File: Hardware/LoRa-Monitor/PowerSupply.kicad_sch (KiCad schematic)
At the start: 0 parts

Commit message: Fixed Power and Ground on the Interface nodes
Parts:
- added U8: IRM-03-5, Converter_ACDC:Converter_ACDC_MeanWell_IRM-03-xx_THT, symbol Converter_ACDC:IRM-03-5
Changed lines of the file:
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@@
 	(generator_version "10.0")
 	(paper "A4")
+	(symbol
+		(lib_id "Converter_ACDC:IRM-03-5")
+		(at 67.31 53.34 0)
+		(unit 1)
+		(body_style 1)
+		(exclude_from_sim no)
+		(in_bom yes)
+		(on_board yes)
+		(in_pos_files yes)
+		(dnp no)
+		(fields_autoplaced yes)
+		(property "Reference" "U8"
+			(at 67.31 43.18 0)
+			(show_name no)
+			(do_not_autoplace no)
+			(effects
+				(font
+					(size 1.27 1.27)
+				)
+			)
+		)
+		(property "Value" "IRM-03-5"
+			(at 67.31 45.72 0)
+			(show_name no)
+			(do_not_autoplace no)
+			(effects
+				(font
+					(size 1.27 1.27)
+				)
+			)
+		)
+		(property "Footprint" "Converter_ACDC:Converter_ACDC_MeanWell_IRM-03-xx_THT"
+			(at 67.31 62.23 0)
+			(hide yes)
+			(show_name no)
+			(do_not_autoplace no)
+			(effects
+				(font
+					(size 1.27 1.27)
+				)
+			)
+		)
+		(property "Datasheet" "https://www.meanwell.com/Upload/PDF/IRM-03/IRM-03-SPEC.PDF"
+			(at 67.31 63.5 0)
+			(hide yes)
+			(show_name no)
+			(do_not_autoplace no)
+			(effects
+				(font
+					(size 1.27 1.27)
+				)
+			)
+		)
+		(property "Description" "5V, 600mA, 3W, Isolated, AC-DC, IRM03"
+			(at 67.31 53.34 0)
+			(hide yes)
+			(show_name no)
+			(do_not_autoplace no)
+			(effects
+				(font
+					(size 1.27 1.27)
+				)
+			)
+		)
+		(pin "3"
+		)
+		(pin "1"
+		)
+		(pin "16"
+		)
+		(pin "14"
+		)
+		(pin "5"
+		)
+		(instances
+			(project "LoRa-Monitor"
+				(path "/7510cc7d-c141-46d4-8947-7def3af8cf35/e98113b5-abe6-4cd1-ae05-96bff57301ff"
+					(reference "U8")
+					(unit 1)
+				)
+			)
+		)
+	)
 )

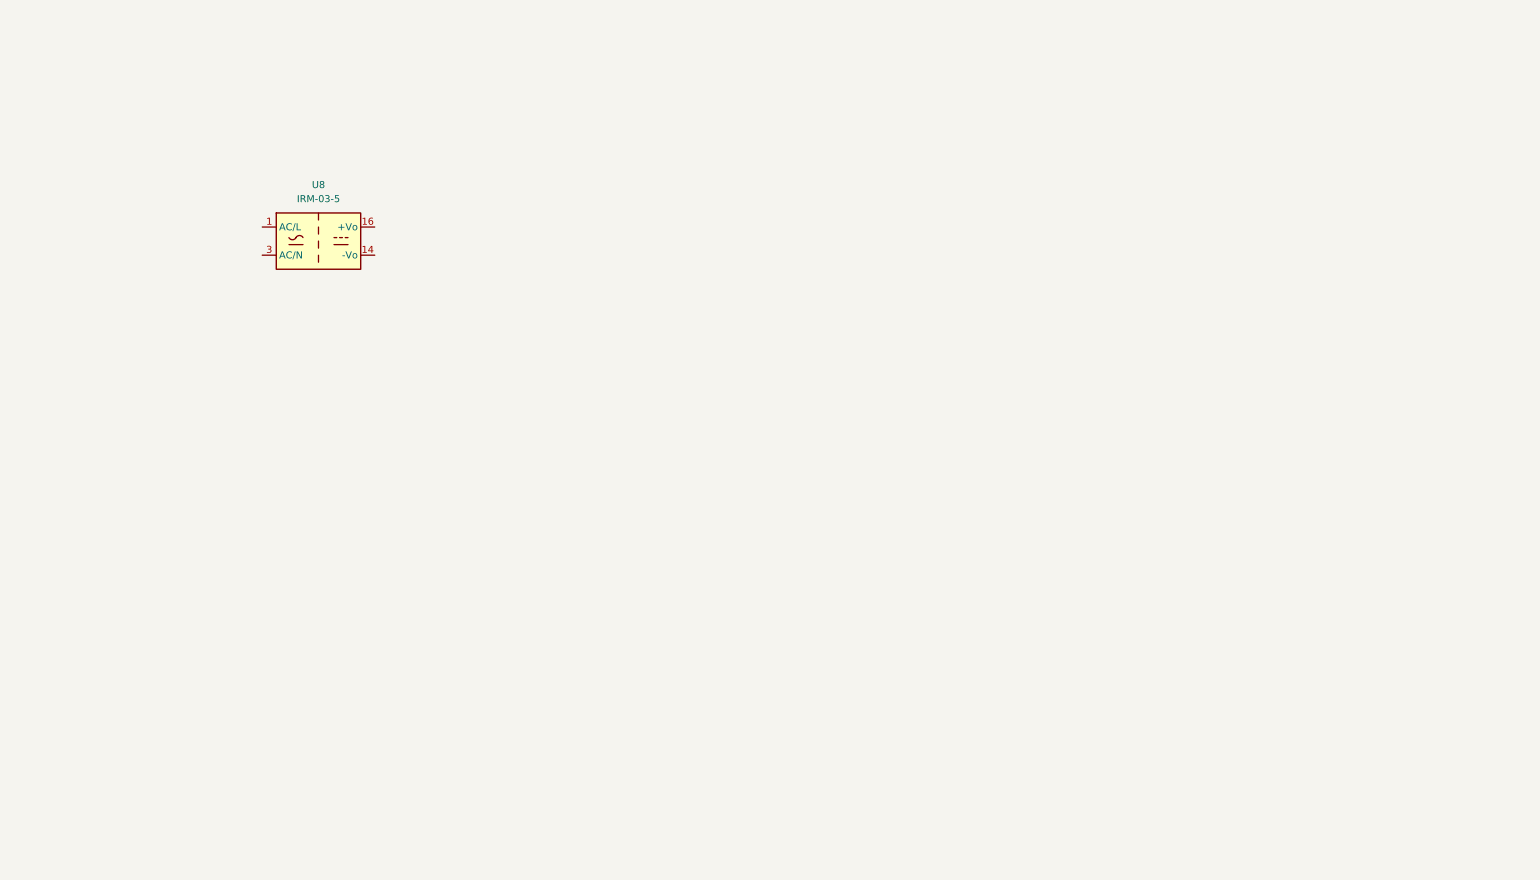
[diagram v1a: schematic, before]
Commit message: Added PSU
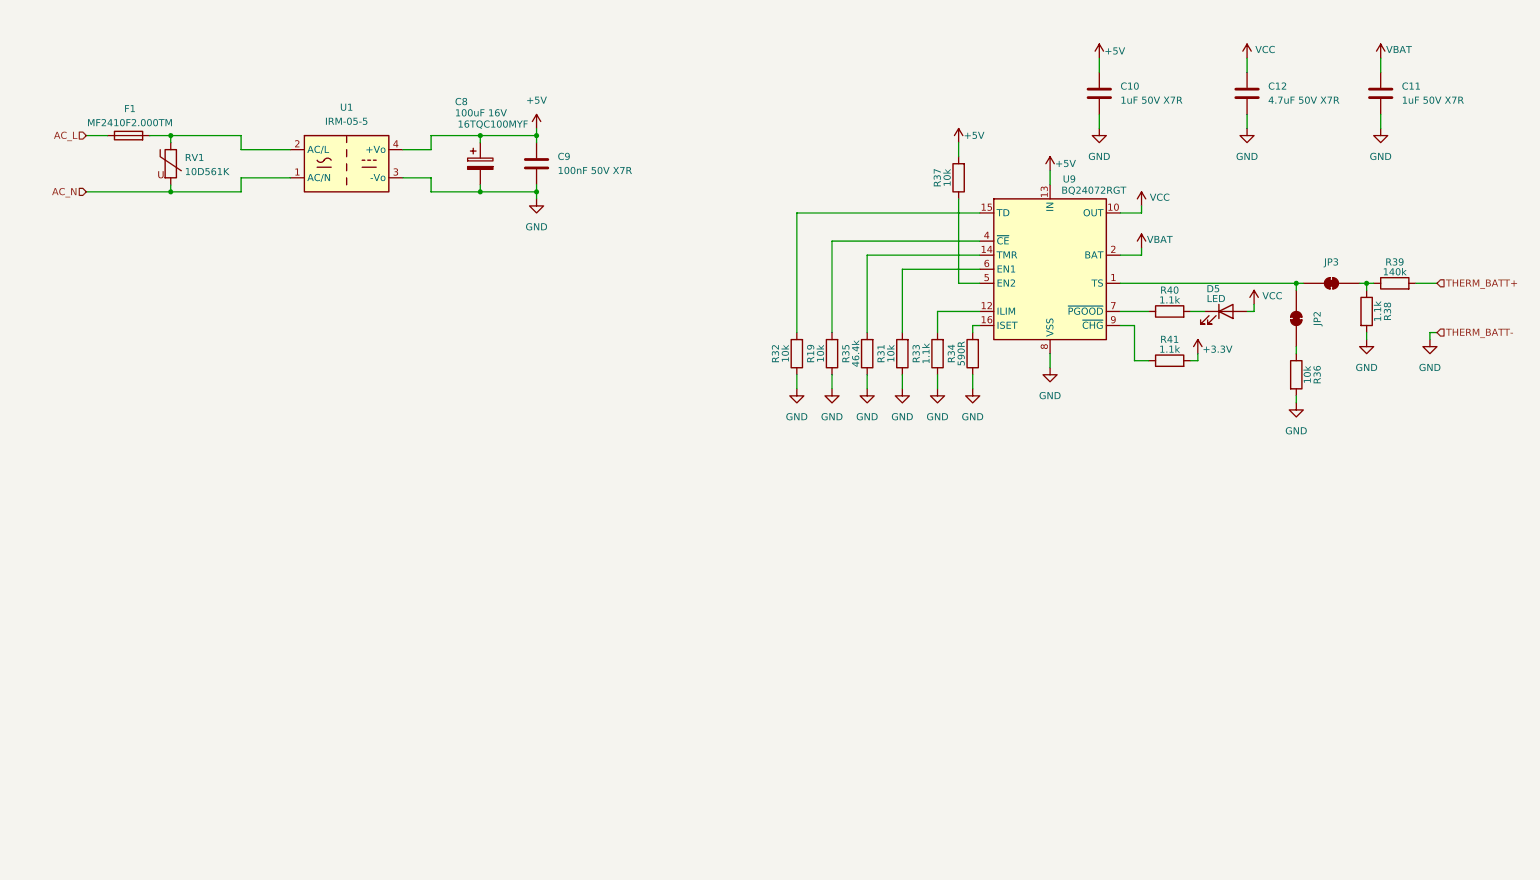
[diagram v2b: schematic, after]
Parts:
- removed U8: IRM-03-5, Converter_ACDC:Converter_ACDC_MeanWell_IRM-03-xx_THT, symbol Converter_ACDC:IRM-03-5
- added C10, C11: 1uF 50V X7R, Capacitor_SMD:C_0805_2012Metric, symbol Device:C
- added C12: 4.7uF 50V X7R, Capacitor_SMD:C_0805_2012Metric, symbol Device:C
- added C8: 100uF 16V, Capacitor_Tantalum_SMD:CP_EIA-7343-31_Kemet-D, symbol Device:C_Polarized
- added C9: 100nF 50V X7R, Capacitor_SMD:C_0805_2012Metric, symbol Device:C
- added D5: LED, LED_SMD:LED_0805_2012Metric, symbol Device:LED
- added F1: MF2410F2.000TM, DeviceComponents:Fuse_2410_6125Metric, symbol Device:Fuse
- added JP2, JP3: SolderJumper_2_Bridged, Jumper:SolderJumper-2_P1.3mm_Bridged_RoundedPad1.0x1.5mm, symbol Jumper:SolderJumper_2_Bridged
- added R19, R31, R32, R36, R37: 10k, Resistor_SMD:R_0805_2012Metric, symbol Device:R
- added R33, R38, R40, R41: 1.1k, Resistor_SMD:R_0805_2012Metric, symbol Device:R
- added R34: 590R, Resistor_SMD:R_0805_2012Metric, symbol Device:R
- added R35: 46.4k, Resistor_SMD:R_0805_2012Metric, symbol Device:R
- added R39: 140k, Resistor_SMD:R_0805_2012Metric, symbol Device:R
- added RV1: 10D561K, Varistor:RV_Disc_D12mm_W6.1mm_P7.5mm, symbol Device:Varistor
- added U1: IRM-05-5, Converter_ACDC:Converter_ACDC_MeanWell_IRM-05-xx_THT, symbol Converter_ACDC:IRM-05-5
- added U9: BQ24072RGT, Package_DFN_QFN:VQFN-16-1EP_3x3mm_P0.5mm_EP1.6x1.6mm, symbol Battery_Management:BQ24072RGT
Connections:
- new net: JP3.1 (A), R38.1, R39.1
- new net: JP2.1 (A), R36.1
- new net: JP2.2 (B), JP3.2 (B), U9.1 (TS)
- new net: F1.2, RV1.1, U1.2 (AC/L)
- new net: R41.1, U9.9 (~{CHG})
- new net: R40.1, U9.7 (~{PGOOD})
- new net: D5.1 (K), R40.2
- new net: R33.2, U9.12 (ILIM)
- new net: R31.2, U9.6 (EN1)
- new net: R37.1, U9.5 (EN2)
- new net: R35.2, U9.14 (TMR)
- new net: R32.2, U9.15 (TD)
- new net: R34.2, U9.16 (ISET)
- new net: R19.2, U9.4 (~{CE})
- new net +3.3V: R41.2
- new net +5V: C10.1, C8.1, C9.1, R37.2, U1.4 (+Vo), U9.13 (IN)
- new net AC_L: F1.1
- new net AC_N: RV1.2, U1.1 (AC/N)
- new net GND: C10.2, C11.2, C12.2, C8.2, C9.2, R19.1, R31.1, R32.1, R33.1, R34.1, R35.1, R36.2, R38.2, U1.3 (-Vo), U9.17 (VSS), U9.8 (VSS)
- new net THERM_BATT+: R39.2
- new net VBAT: C11.1, U9.2 (BAT), U9.3 (BAT)
- new net VCC: C12.1, D5.2 (A), U9.10 (OUT), U9.11 (OUT)

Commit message: Added more PSU components.
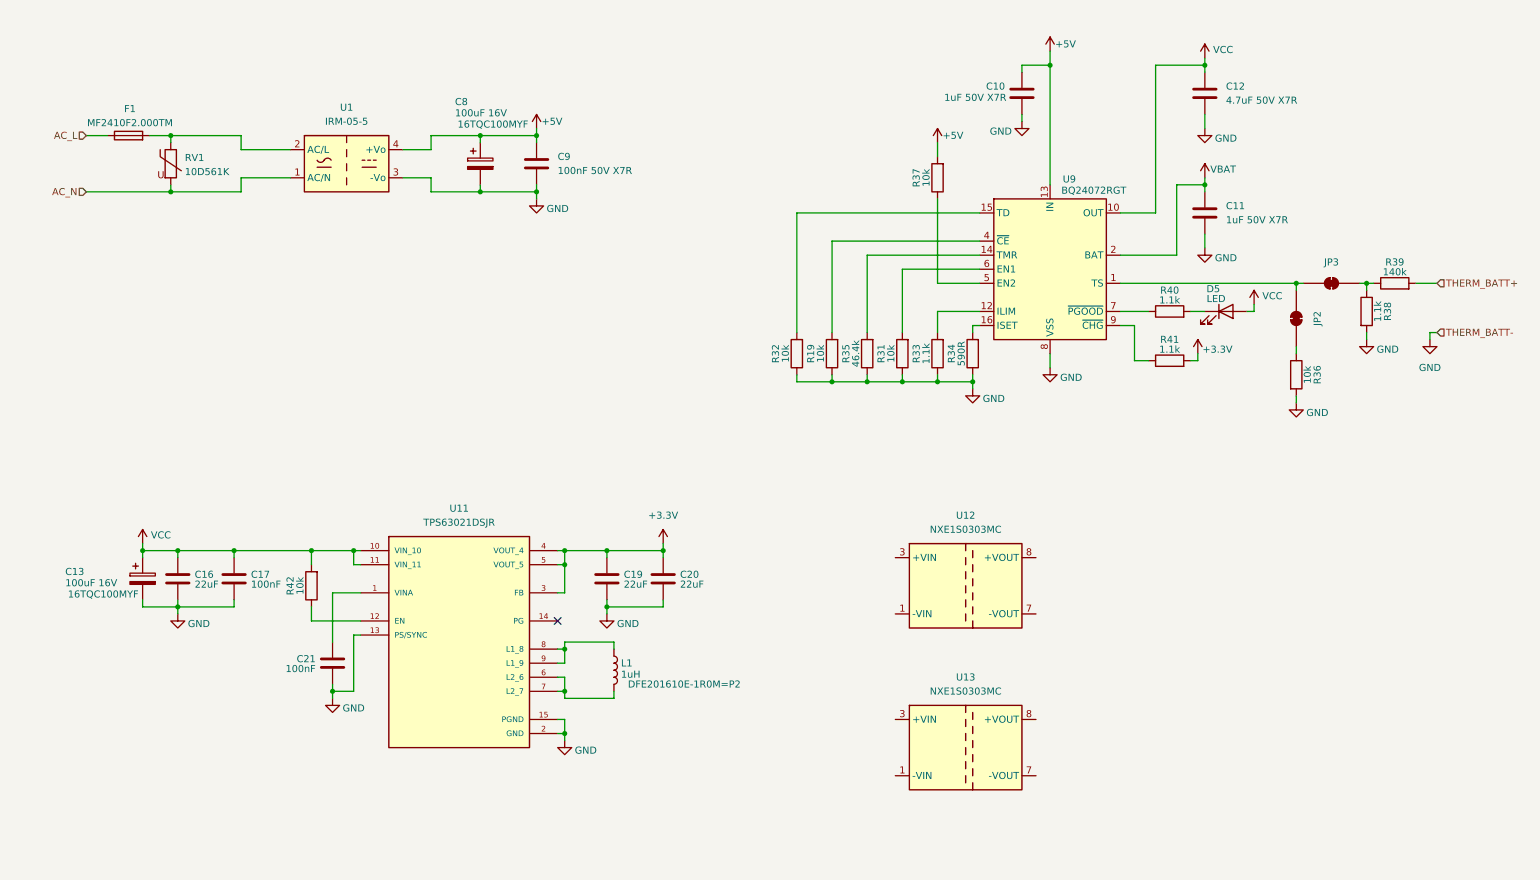
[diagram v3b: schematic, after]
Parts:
- added C13: 100uF 16V, Capacitor_Tantalum_SMD:CP_EIA-7343-31_Kemet-D, symbol Device:C_Polarized
- added C16, C19, C20: 22uF, Capacitor_SMD:C_0805_2012Metric, symbol Device:C
- added C17, C21: 100nF, Capacitor_SMD:C_0805_2012Metric, symbol Device:C
- added L1: 1uH, DeviceComponents:L_0806_2016Metric, symbol Device:L
- added R42: 10k, Resistor_SMD:R_0805_2012Metric, symbol Device:R
- added U11: TPS63021DSJR, symbol DeviceComponents:TPS63021DSJR
- added U12, U13: NXE1S0303MC, Converter_DCDC:Converter_DCDC_Murata_NXExSxxxxMC_SMD, symbol Regulator_Switching:NXE1S0303MC
- U1: footprint Converter_ACDC:Converter_ACDC_MeanWell_IRM-05-xx_THT -> DeviceComponents:Converter_ACDC_MeanWell_IRM-05-xx_THT
- U9: footprint Package_DFN_QFN:VQFN-16-1EP_3x3mm_P0.5mm_EP1.6x1.6mm -> DeviceComponents:VQFN-16-1EP_3x3mm_P0.5mm_EP1.6x1.6mm
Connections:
- net +3.3V: now also C19.1, C20.1, U11.3 (FB), U11.4 (VOUT_4), U11.5 (VOUT_5)
- net GND: now also C13.2, C16.2, C17.2, C19.2, C20.2, C21.2, U11.13 (PS/SYNC), U11.15 (PGND), U11.2 (GND)
- net VCC: now also C13.1, C16.1, C17.1, R42.2, U11.10 (VIN_10), U11.11 (VIN_11)
- new net: C21.1, U11.1 (VINA)
- new net: R42.1, U11.12 (EN)
- new net: L1.2, U11.6 (L2_6), U11.7 (L2_7)
- new net: L1.1, U11.8 (L1_8), U11.9 (L1_9)
- no-connect marks 0 -> 1
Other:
- moved on the sheet: C10, C11, C12, R37

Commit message: Finished PSU module, started Energy meter
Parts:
- added C14, C15: 10uF, Capacitor_SMD:C_0805_2012Metric, symbol Device:C
- added C18, C22: 1uF, Capacitor_SMD:C_0805_2012Metric, symbol Device:C
- added L2, L3: 15uH, DeviceComponents:L_0806_2016Metric, symbol Device:L
- U11: footprint (none) -> DeviceComponents:IC_TPS63021DSJR
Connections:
- net +3.3V: now also U12.3 (+VIN), U13.3 (+VIN), C18.1, C22.1
- net GND: now also U12.1 (-VIN), U13.1 (-VIN), C18.2, C22.2
- net GND_485: now reaches U13.7 (-VOUT)
- net GND_485: now also U12.7 (-VOUT), C14.2, C15.2
- net at U13.8 (+VOUT): now also L3.1
- net at U12.8 (+VOUT): now also L2.1
- new net +3.3V_485: C14.1, C15.1, L2.2, L3.2
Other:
- moved on the sheet: C13, C16, C17, C19, C20, C21, C8, C9, F1, L1, R42, RV1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

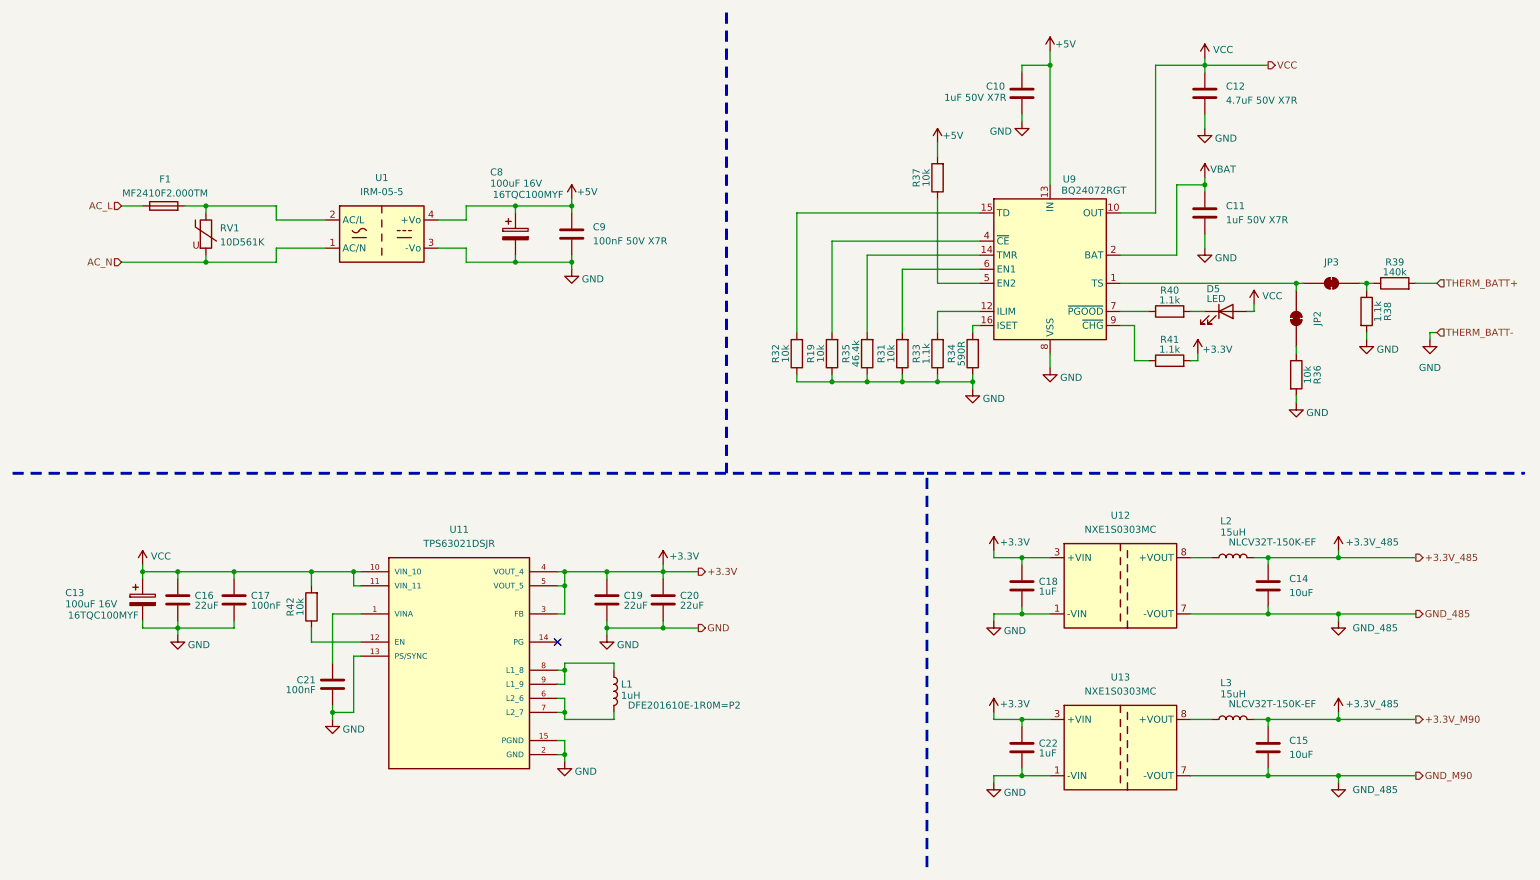
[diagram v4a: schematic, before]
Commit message: Finished schematic, started with PCB design
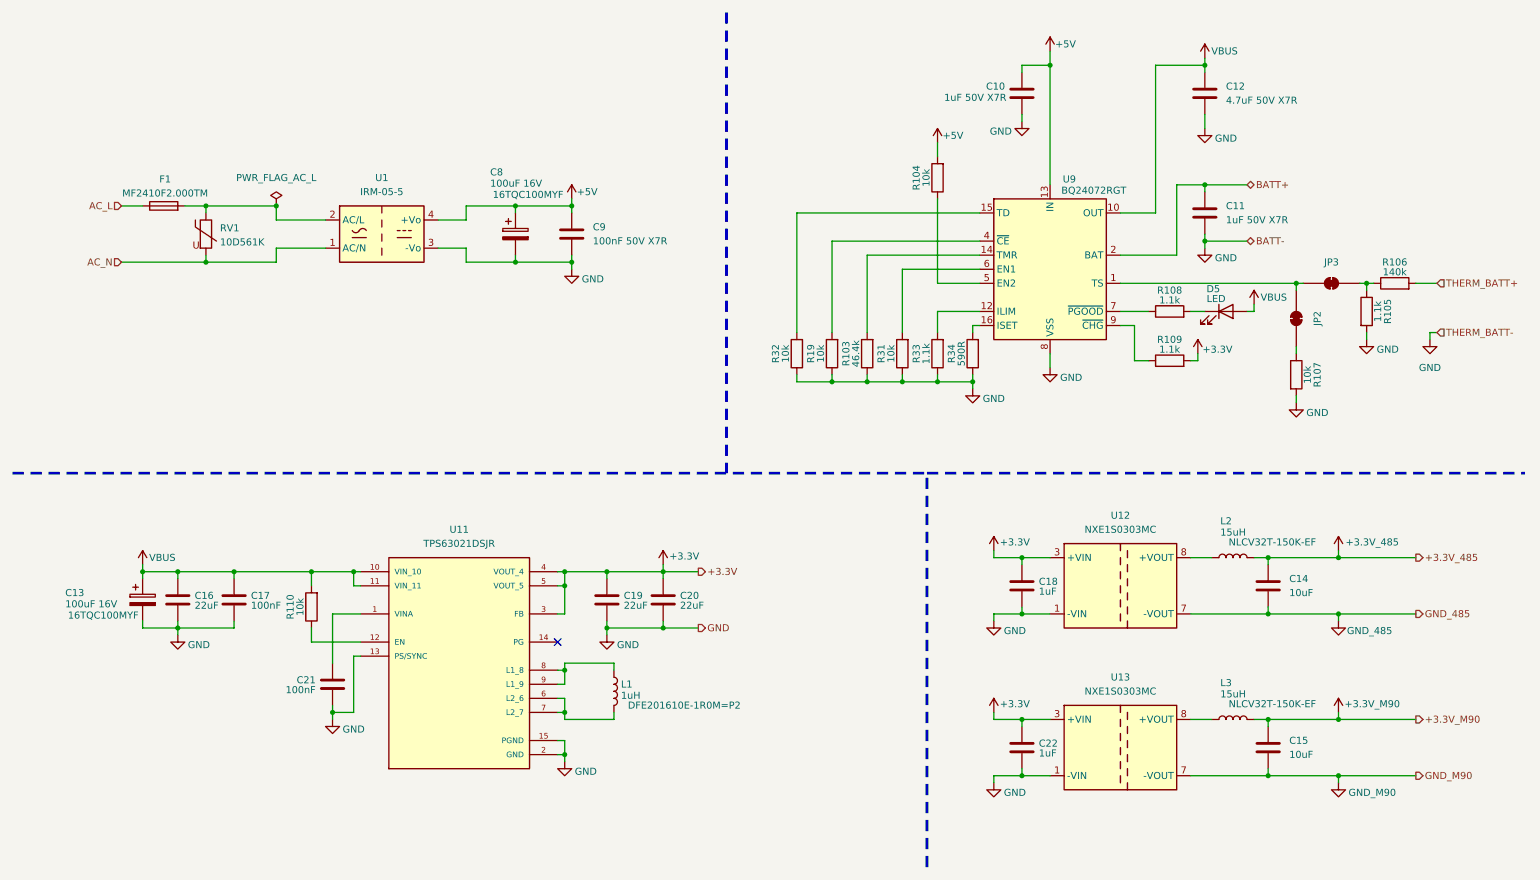
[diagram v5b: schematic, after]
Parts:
- removed R35: 46.4k, Resistor_SMD:R_0805_2012Metric, symbol Device:R
- removed R36, R37, R42: 10k, Resistor_SMD:R_0805_2012Metric, symbol Device:R
- removed R38, R40, R41: 1.1k, Resistor_SMD:R_0805_2012Metric, symbol Device:R
- removed R39: 140k, Resistor_SMD:R_0805_2012Metric, symbol Device:R
- added R103: 46.4k, Resistor_SMD:R_0805_2012Metric, symbol Device:R
- added R104, R107, R110: 10k, Resistor_SMD:R_0805_2012Metric, symbol Device:R
- added R105, R108, R109: 1.1k, Resistor_SMD:R_0805_2012Metric, symbol Device:R
- added R106: 140k, Resistor_SMD:R_0805_2012Metric, symbol Device:R
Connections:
- net +3.3V: now also R109.2
- net +3.3V_485: no longer C15.1, L3.2
- net +5V: now also R104.2
- net GND: now also U11.16 (GND), U11.17 (GND), U11.18 (GND), U11.19 (GND), U11.20 (GND), U11.21 (GND), U11.22 (GND), U11.23 (GND), U11.24 (GND), U11.25 (GND), U11.26 (GND), U11.27 (GND), U11.28 (GND), U11.29 (GND), U11.30 (GND), R103.1, R105.2, R107.2
- net GND_485: no longer C15.2, U13.7 (-VOUT)
- net THERM_BATT+: now also R106.2
- net at U11.12 (EN): now also R110.1
- net at JP3.1 (A): now also R105.1, R106.1
- net at JP2.1 (A): now also R107.1
- net at U9.9 (~{CHG}): now also R109.1
- net at U9.7 (~{PGOOD}): now also R108.1
- net at D5.1 (K): now also R108.2
- net at U9.5 (EN2): now also R104.1
- net at U9.14 (TMR): now also R103.2
- net VBAT renamed BATT+
- net VCC renamed VBUS
- net VBUS: now also R110.2
- new net +3.3V_M90: C15.1, L3.2
- new net GND_M90: C15.2, U13.7 (-VOUT)
